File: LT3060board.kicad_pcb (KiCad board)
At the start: 2 copper layers, 7.6 x 14.2 mm, 6 parts, among them IC1 LT3060-TSOT, K1 CONN_3

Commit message: more nice
Signed-off-by: Stefan Helmert <stefan.helmert@t-online.de>
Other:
- board text added: "100 mA"
- board text added: "LT3060"
- board text added: "entroserv.de"
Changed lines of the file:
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@@
     (links 14)
     (no_connects 0)
-    (area 52.2335 47.0011 64.286177 63.550001)
+    (area 50.847286 47.0011 64.286177 65.1272)
     (thickness 1.6)
-    (drawings 5)
+    (drawings 8)
     (tracks 24)
     (zones 0)
@@
     (visible_elements 7FFFFFFF)
     (pcbplotparams
-      (layerselection 3178497)
+      (layerselection 284196865)
       (usegerberextensions true)
       (excludeedgelayer true)
@@
       (outputformat 1)
       (mirror false)
-      (drillshape 1)
+      (drillshape 0)
       (scaleselection 1)
       (outputdirectory ""))
@@
     )
   )
+  (gr_text entroserv.de (at 55.88 54.483 270) (layer B.SilkS)
+    (effects (font (size 0.8 0.8) (thickness 0.15)) (justify mirror))
+  )
+  (gr_text LT3060 (at 57.15 62.23) (layer B.SilkS)
+    (effects (font (size 1.2 1.2) (thickness 0.3)) (justify mirror))
+  )
+  (gr_text "100 mA" (at 54.483 54.864 270) (layer B.SilkS)
+    (effects (font (size 1.2 1.2) (thickness 0.3)) (justify mirror))
+  )
   (gr_line (start 53.34 63.5) (end 53.34 49.276) (angle 90) (layer Edge.Cuts) (width 0.1))
   (gr_line (start 60.96 63.5) (end 53.34 63.5) (angle 90) (layer Edge.Cuts) (width 0.1))
   (gr_line (start 60.96 49.276) (end 60.96 63.5) (angle 90) (layer Edge.Cuts) (width 0.1))
   (gr_line (start 53.34 49.276) (end 60.96 49.276) (angle 90) (layer Edge.Cuts) (width 0.1))
-  (gr_text 3V3 (at 56.896 54.483 270) (layer B.SilkS)
+  (gr_text 3V3 (at 58.039 53.594 270) (layer B.SilkS)
     (effects (font (size 3 3) (thickness 0.3)) (justify mirror))
   )

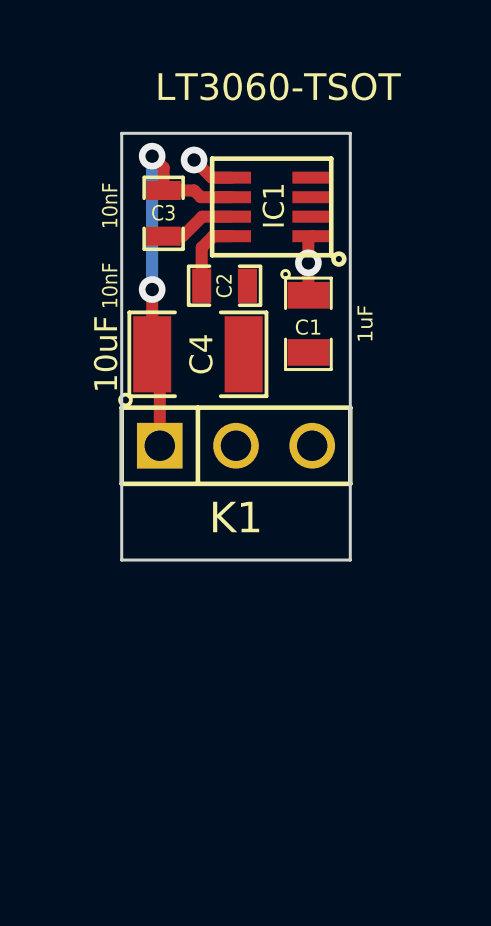
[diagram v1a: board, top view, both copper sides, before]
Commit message: Version with 3 TVS-diodes for protection.
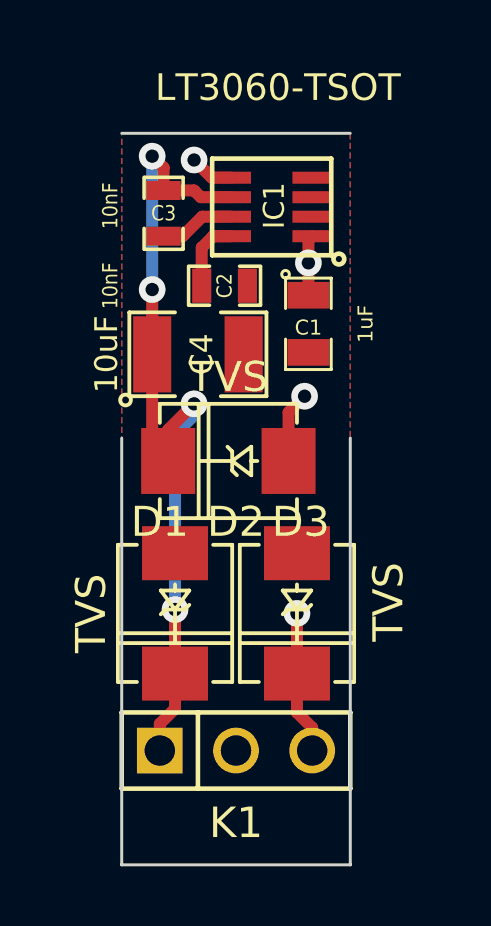
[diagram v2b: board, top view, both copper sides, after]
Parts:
- added D1: TVS, DO-214AA(SMB), F.Cu at (59.2, 65.3)
- added D2: TVS, DO-214AA(SMB), F.Cu at (56.9, 60.2)
- added D3: TVS, DO-214AA(SMB), F.Cu at (55.1, 65.3)
- moved K1 10.2 mm to (57.1, 69.8)
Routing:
- net /Vout: track 13.4 -> 28.3 mm, vias 2 -> 4
- net /Vin: track 3.50 -> 10.7 mm, vias 2 -> 4
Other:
- board size 7.6 x 14.2 mm -> 7.6 x 24.4 mm
- board text added: "I"
- board text added: "O"
- board text added: "T"
